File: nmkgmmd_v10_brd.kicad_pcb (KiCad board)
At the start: 2 copper layers, 85 x 69 mm, 148 parts, among them J1 CONN_01X05, J10 CONN_01X10, J14 CONN_01X10, J15 CONN_01X01, J16 CONN_01X01, J17 CONN_01X01, J18 CONN_01X01, J2 CONN_01X03, J20 CONN_01X10, J21 CONN_01X01, J22 CONN_01X01, J23 CONN_01X01, J24 CONN_01X01, J3 CONN_01X03, J4 CONN_01X04, J5 CONN_01X04, J6 CONN_01X04, J7 CONN_01X03, J8 CONN_01X03, J9 CONN_01X10, Q1 BSS138PS, Q10 PSMN1R0-40YLD, Q11 PSMN1R0-40YLD, Q12 PSMN1R0-40YLD, Q13 PSMN1R0-40YLD, Q14 PSMN1R0-40YLD, Q15 PSMN1R0-40YLD, Q16 PSMN1R0-40YLD, Q17 PSMN1R0-40YLD, Q2 PSMN1R0-40YLD, Q3 PSMN1R0-40YLD, Q4 PSMN1R0-40YLD, Q5 PSMN1R0-40YLD, Q6 PSMN1R0-40YLD, Q7 PSMN1R0-40YLD, Q8 PSMN1R0-40YLD, Q9 PSMN1R0-40YLD, SW1 SKRPACE010, SW2 SW_DPDT_x2, U1 STM32F303CCTx, U2 MCP16301, U3 MCP16301, U4 A4957, U5 ACS711, U6 A4957, U7 ACS711, Y1 Crystal

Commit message: 進捗，セーブ
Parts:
- added C33: C, Capacitors_SMD:C_0603, F.Cu at (61.0, 153.0)
- added C34: C, Capacitors_SMD:C_0603, F.Cu at (59.0, 153.0)
- added C35: C, Capacitors_SMD:C_0603, F.Cu at (63.0, 153.0)
- added C36: C, Capacitors_SMD:C_0603, F.Cu at (47.0, 105.0)
- added C37: C, Capacitors_SMD:C_0603, F.Cu at (47.0, 107.0)
- added C38: C, Capacitors_SMD:C_0603, F.Cu at (47.0, 103.0)
- C1, C10, C11, C12, C13, C14, C15, C16, C20, C31, C4, C5, C7, C8, C9, D1, D2, D6, D7, D8, D9, L3, L4, R1, R14, R15, R16, R17, R18, R19, R2, R27, R28, R29, R30, R31, R32, U2, U3: moved to B.Cu
- C23: moved to F.Cu
- J1: footprint Connectors_JST:JST_ZH_S05B-ZR_05x1.50mm_Angled -> Connectors_JST:JST_SH_BM05B-SRSS-TB_05x1.00mm_Straight; moved to B.Cu
- J6: footprint Connectors_JST:JST_ZH_S04B-ZR_04x1.50mm_Angled -> Connectors_JST:JST_ZH_B04B-ZR_04x1.50mm_Straight; moved to B.Cu
- moved R18 81.4 mm to (77.4, 151.2), turned to 180 degrees
- moved R17 80.2 mm to (80.0, 151.2), turned to 180 degrees
- moved R16 78.3 mm to (77.4, 141.2), turned to 180 degrees
- moved R13 76.0 mm to (91.8, 153.2), turned to 0 degrees
- moved C14 74.3 mm to (81.9, 148.6)
- moved C12 73.6 mm to (76.7, 148.4), turned to 270 degrees
- moved R15 70.5 mm to (80.0, 141.2), turned to 180 degrees
- moved C16 69.4 mm to (87.0, 151.0), turned to 0 degrees
- moved C11 68.9 mm to (76.7, 138.6), turned to 270 degrees
- moved R14 68.5 mm to (92.3, 150.9), turned to 270 degrees
- moved U3 68.3 mm to (79.4, 148.6)
- moved D9 68.0 mm to (83.2, 151.0), turned to 0 degrees
- moved C1 67.5 mm to (76.8, 98.7), turned to 0 degrees
- moved C13 66.4 mm to (81.9, 138.6)
- moved D8 65.9 mm to (83.2, 141.0), turned to 0 degrees
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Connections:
- R4 pad 2: Net-(J3-Pad3) -> Net-(J2-Pad3)
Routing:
- net GND: track 151.6 -> 242.9 mm, vias 50 -> 59
- net V_BATT: track 108.6 -> 176.4 mm, vias 1 -> 4
- net /MCU/T3_CH1: track 0.00 -> 48.5 mm
- net /MCU/T3_CH2: track 0.00 -> 47.1 mm, vias 0 -> 1
- net /MCU/T8_CH2N: track 0.00 -> 38.4 mm, vias 0 -> 1
- net Net-(SW2-Pad2): track 0.00 -> 35.8 mm, vias 0 -> 3
- net /MCU/A1_IN2: track 0.00 -> 35.7 mm, vias 0 -> 1
- net /MCU/FAULT2: track 0.00 -> 33.9 mm, vias 0 -> 3
- net /MCU/T8_CH1N: track 0.00 -> 33.6 mm, vias 0 -> 1
- net /MCU/A1_IN1: track 0.00 -> 32.1 mm, vias 0 -> 1
- net /MCU/T1_CH2: track 0.00 -> 27.9 mm, vias 0 -> 1
- net NRST: track 0.00 -> 27.6 mm, vias 0 -> 2
- net /MCU/T1_CH1: track 0.00 -> 26.9 mm, vias 0 -> 1
- net +3V3: track 56.2 -> 81.6 mm
- net /MCU/A3_IN1: track 0.00 -> 24.8 mm, vias 0 -> 1
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- added copper zone on B.Cu, net +3V3
- added copper zone on B.Cu, net +5V
- added copper zone on B.Cu, net Net-(C13-Pad1)
- added copper zone on B.Cu, net Net-(C13-Pad2)
- added copper zone on B.Cu, net Net-(C14-Pad1)
- added copper zone on B.Cu, net Net-(C14-Pad2)
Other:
- outline, holes or cut-outs redrawn

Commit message: 進捗
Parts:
- L1: moved to B.Cu
- R14: moved to F.Cu
- moved L1 36.4 mm to (105.4, 104.6)
- moved J3 33.0 mm to (105.4, 135.8)
- moved J7 33.0 mm to (105.4, 102.8)
- moved J2 33.0 mm to (105.4, 142.4)
- moved J8 33.0 mm to (105.4, 109.4)
- moved C12 16.7 mm to (88.2, 136.3)
- moved C14 16.7 mm to (93.4, 136.5)
- moved C16 16.7 mm to (98.5, 138.9)
- moved D1 16.7 mm to (101.0, 138.3)
- moved D7 16.7 mm to (90.0, 133.4)
- moved D9 16.7 mm to (94.8, 138.9)
- moved L4 16.7 mm to (97.1, 135.0)
- moved R1 16.7 mm to (101.0, 135.6)
- moved R17 16.7 mm to (91.5, 139.2)
- moved R18 16.7 mm to (88.9, 139.2)
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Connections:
- J3 pad 1: +5V -> GND
- J3 pad 2: GND -> +5V
- J5 pad 2: /MCU/T3_CH1 -> /MCU/T3_CH2
- J5 pad 3: /MCU/T3_CH2 -> /MCU/T3_CH1
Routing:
- net +5V: track 13.3 -> 57.7 mm, vias 0 -> 1
- net Net-(J2-Pad3): track 0.00 -> 41.6 mm, vias 0 -> 1
- net /MCU/A1_IN2: track 35.7 -> 1.50 mm, vias 1 -> 0
- net /MCU/A1_IN1: track 32.1 -> 2.31 mm
- net GND: track 242.9 -> 261.5 mm
- net Net-(J3-Pad3): track 0.00 -> 18.2 mm
- net +3V3: track 81.6 -> 92.8 mm, vias 2 -> 3
- net Net-(J7-Pad2): track 2.40 -> 9.75 mm
- net Net-(R22-Pad1): track 0.00 -> 6.00 mm
- net V_BATT: track 176.4 -> 181.3 mm, vias 4 -> 5
- net Net-(C14-Pad2): track 3.80 -> 8.53 mm
- net /MCU/FAULT1: track 21.6 -> 19.6 mm
- net /MCU/T1_CH1: track 26.9 -> 24.9 mm
- net /MCU/T3_CH1: track 48.5 -> 46.7 mm
- net Net-(SW2-Pad2): track 35.8 -> 37.4 mm
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- added copper zone on F.Cu, net Net-(C21-Pad2)
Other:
- board text added: "+5V"
- board text added: "GND"

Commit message: 進捗
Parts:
- C6, R7, R8, R9: moved to B.Cu
- moved J1 18.7 mm to (101.0, 92.0), turned to 180 degrees
- moved SW1 17.1 mm to (93.5, 91.1), turned to 180 degrees
- moved C1 16.2 mm to (92.2, 93.8), turned to 180 degrees
- moved C5 6.91 mm to (99.9, 111.9)
- moved C4 6.91 mm to (101.3, 111.9)
- moved C7 6.90 mm to (97.2, 103.1)
- moved C8 6.90 mm to (87.9, 105.7)
- moved U1 6.90 mm to (93.9, 109.0)
- moved R12 6.79 mm to (101.8, 109.3), turned to 180 degrees
- moved D3 6.50 mm to (102.1, 121.7), turned to 90 degrees
- moved D4 6.50 mm to (100.6, 121.7), turned to 90 degrees
- moved D5 6.50 mm to (99.1, 121.7), turned to 90 degrees
- moved C6 3.94 mm to (99.1, 114.9), turned to 180 degrees
- moved R7 3.92 mm to (102.1, 118.9), turned to 270 degrees
- moved R8 3.92 mm to (100.6, 118.9), turned to 270 degrees
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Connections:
- J4 pad 2: /MCU/T2_CH1 -> /MCU/T2_CH2
- J4 pad 3: /MCU/T2_CH2 -> /MCU/T2_CH1
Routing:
- net +3V3: track 92.8 -> 132.1 mm, vias 3 -> 4
- net /MCU/A1_IN2: track 1.50 -> 37.1 mm, vias 0 -> 2
- net /MCU/RESET2: track 2.04 -> 21.9 mm, vias 1 -> 3
- net Net-(J2-Pad3): track 41.6 -> 24.2 mm, vias 1 -> 0
- net /MCU/T1_CH1N: track 8.12 -> 22.3 mm, vias 1 -> 3
- net /MCU/LED1: track 13.9 -> 0.00 mm, vias 1 -> 0
- net /MCU/A1_IN1: track 2.31 -> 15.5 mm, vias 1 -> 2
- net Net-(R12-Pad2): track 9.05 -> 2.94 mm
- net /MCU/T2_CH1: track 18.2 -> 13.3 mm, vias 2 -> 1
- net /MCU/LED0: track 16.4 -> 13.2 mm, vias 1 -> 2
- net /MCU/T1_CH2N: track 23.9 -> 20.8 mm
- net /MCU/T1_CH1: track 24.9 -> 22.0 mm
- net /MCU/FAULT1: track 19.6 -> 17.1 mm
- net /MCU/T2_CH2: track 17.1 -> 14.5 mm, vias 0 -> 1
- net NRST: track 27.6 -> 30.1 mm
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- added copper zone on F.Cu, net Net-(C22-Pad2)
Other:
- board text added: "+3V3"
- board text added: "AN1"
- board text added: "AN2"

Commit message: 進捗
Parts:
- R10, R11: moved to B.Cu
- moved R10 101.4 mm to (169.1, 69.4), turned to 270 degrees
- moved R11 99.5 mm to (169.1, 72.0), turned to 270 degrees
- moved J6 97.1 mm to (170.0, 84.5)
- moved L2 96.1 mm to (175.9, 83.7)
- moved C9 96.1 mm to (177.8, 84.5)
- moved C10 96.1 mm to (179.2, 84.5)
- moved C2 95.6 mm to (181.6, 89.2), turned to 90 degrees
- moved Y1 94.8 mm to (182.3, 86.0)
- moved J8 94.3 mm to (191.4, 70.8)
- moved C8 92.8 mm to (174.8, 73.0), turned to 45 degrees
- moved C7 92.7 mm to (184.3, 71.5), turned to 315 degrees
- moved C4 92.1 mm to (187.7, 79.9)
- moved C5 92.1 mm to (186.3, 79.9)
- moved C6 92.1 mm to (185.5, 82.9)
- moved U1 92.1 mm to (180.3, 77.0)
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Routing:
- net GND: track 259.2 -> 315.4 mm, vias 60 -> 75
- net /MCU/A3_IN1: track 24.8 -> 5.33 mm, vias 1 -> 0
- net V_BATT: track 181.3 -> 200.1 mm, vias 5 -> 4
- net /MCU/A1_IN2: track 37.1 -> 21.9 mm
- net +3V3: track 132.1 -> 146.4 mm
- net /MCU/LED1: track 0.00 -> 12.0 mm, vias 0 -> 2
- net /MCU/LED2: track 7.77 -> 14.5 mm, vias 0 -> 2
- net /MCU/RESET2: track 21.9 -> 27.9 mm, vias 3 -> 1
- net /MCU/T1_CH2: track 24.4 -> 19.1 mm
- net /MCU/T1_CH1: track 22.0 -> 17.3 mm
- net /MCU/T1_CH2N: track 20.8 -> 16.7 mm
- net /MCU/FAULT1: track 17.1 -> 13.0 mm
- net /MCU/LED0: track 13.2 -> 17.2 mm
- net /MCU/T8_CH1N: track 34.5 -> 30.6 mm
- net /MCU/T8_CH2N: track 37.8 -> 34.1 mm
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
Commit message: ネットリスト更新，進捗
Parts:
- moved C10 1.00 mm to (179.2, 83.5)
- moved C4 1.00 mm to (187.7, 78.9)
- moved C5 1.00 mm to (186.3, 78.9)
- moved C6 1.00 mm to (185.5, 81.9)
- moved C7 1.00 mm to (184.3, 70.5)
- moved C8 1.00 mm to (174.8, 72.0)
- moved C9 1.00 mm to (177.8, 83.5)
- moved L2 1.00 mm to (175.9, 82.7)
- moved R12 1.00 mm to (187.1, 76.2)
- moved U1 1.00 mm to (180.3, 76.0)
- moved Y1 1.00 mm to (182.3, 85.0)
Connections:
- J10 pad 1: /MCU/A2_IN12 -> /MCU/A3_IN1
- J9 pad 1: /MCU/A3_IN1 -> /MCU/A2_IN12
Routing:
- net /MCU/A2_IN12: track 0.00 -> 16.8 mm, vias 0 -> 1
- net /MCU/A3_IN1: track 5.33 -> 20.4 mm, vias 0 -> 1
- net GND: track 315.4 -> 325.1 mm, vias 75 -> 77
- net /MCU/T8_CH1N: track 30.6 -> 27.9 mm
- net /MCU/A1_IN2: track 21.9 -> 19.8 mm, vias 2 -> 1
- net /MCU/T8_CH2N: track 34.1 -> 32.2 mm
- net /MCU/T1_CH1: track 17.3 -> 18.7 mm
- net +3V3: track 146.4 -> 147.8 mm
- net /MCU/T1_CH2: track 19.1 -> 20.5 mm
- net SWCLK: track 17.3 -> 16.2 mm
- net /MCU/T1_CH1N: track 20.7 -> 19.6 mm
- net SWDIO: track 13.0 -> 12.0 mm
- net NRST: track 31.2 -> 30.2 mm
- net /MCU/T8_CH2: track 21.2 -> 22.2 mm
- net /MCU/T8_CH1: track 19.8 -> 20.8 mm
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
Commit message: 進捗
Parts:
- moved Q1 13.0 mm to (170.5, 84.1), turned to 180 degrees
- moved R6 12.7 mm to (173.0, 83.3), turned to 90 degrees
- moved R5 11.7 mm to (168.1, 82.9), turned to 90 degrees
- moved R4 11.0 mm to (170.2, 86.3), turned to 0 degrees
- moved J6 10.5 mm to (170.0, 74.0)
- moved R3 9.14 mm to (168.1, 85.4), turned to 90 degrees
- moved R10 8.04 mm to (177.0, 67.9)
- moved R11 6.77 mm to (174.9, 68.5), turned to 180 degrees
- moved C2 4.77 mm to (177.6, 86.6)
- moved Y1 2.62 mm to (180.3, 86.7)
- moved C3 2.50 mm to (183.0, 86.7)
- moved C16 2.47 mm to (182.2, 106.3)
- moved D9 2.47 mm to (178.3, 106.3)
- moved R18 2.47 mm to (172.5, 106.5)
- moved C14 2.47 mm to (177.0, 103.9)
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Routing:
- net GND: track 325.1 -> 385.2 mm, vias 77 -> 90
- net +5V: track 57.7 -> 102.4 mm
- net Net-(R21-Pad1): track 0.00 -> 26.2 mm
- net Net-(R32-Pad2): track 0.00 -> 23.5 mm
- net /MCU/T15_CH2: track 0.00 -> 22.0 mm, vias 0 -> 1
- net /MCU/T4_CH2: track 1.27 -> 20.6 mm, vias 1 -> 3
- net Net-(J3-Pad3): track 18.2 -> 35.8 mm
- net Net-(J2-Pad3): track 24.2 -> 41.0 mm
- net Net-(R31-Pad2): track 0.00 -> 14.5 mm
- net +3V3: track 147.8 -> 161.2 mm, vias 4 -> 5
- net /MCU/A4_IN3: track 10.7 -> 4.43 mm
- net Net-(R22-Pad1): track 6.00 -> 11.4 mm
- net Net-(Q8-Pad4): track 0.00 -> 3.82 mm, vias 0 -> 1
- net Net-(Q6-Pad4): track 0.00 -> 3.82 mm, vias 0 -> 1
- net /MCU/U2_RX: track 7.09 -> 10.5 mm
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
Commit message: 進捗
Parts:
- added Q18: BSS138, TO_SOT_Packages_SMD:SOT-23, F.Cu at (172.6, 82.6)
- Q1: value BSS138PS -> BSS138; footprint TO_SOT_Packages_SMD:SOT-363_SC-70-6 -> TO_SOT_Packages_SMD:SOT-23
- moved R5 6.17 mm to (169.0, 76.8), turned to 180 degrees
- moved Q1 5.04 mm to (169.0, 79.3), turned to 270 degrees
- moved R4 4.66 mm to (169.0, 81.8), turned to 180 degrees
- moved R3 4.51 mm to (172.6, 85.1), turned to 180 degrees
- moved R6 3.22 mm to (172.6, 80.1), turned to 180 degrees
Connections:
- Q1 pad 1: /MCU/T4_CH2 -> +3V3
- Q1 pad 2: +3V3 -> /MCU/T4_CH2
- R5 pad 2: /MCU/T15_CH2 -> /MCU/T4_CH2
- R6 pad 2: /MCU/T4_CH2 -> /MCU/T15_CH2
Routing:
- net GND: track 385.2 -> 723.1 mm, vias 90 -> 168
- net +5V: track 102.4 -> 110.2 mm, vias 1 -> 4
- net /MCU/T4_CH2: track 20.6 -> 15.3 mm, vias 3 -> 1
- net Net-(J2-Pad3): track 41.0 -> 46.0 mm
- net /MCU/T15_CH2: track 22.0 -> 19.7 mm, vias 1 -> 3
- net +3V3: track 161.2 -> 163.3 mm, vias 5 -> 7
- net Net-(J3-Pad3): track 35.8 -> 36.6 mm
- net Net-(SW2-Pad2): track 36.9 -> 37.5 mm

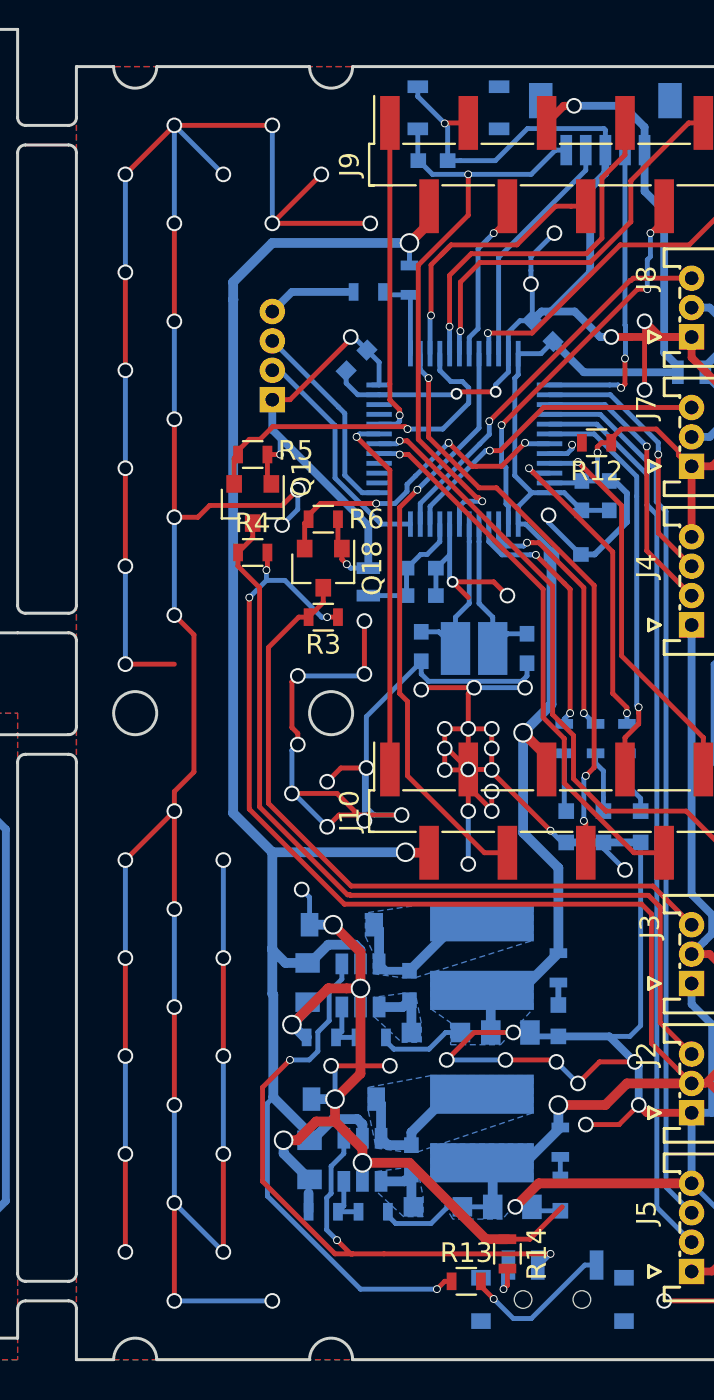
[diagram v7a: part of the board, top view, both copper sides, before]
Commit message: ネットリスト更新 配線編集
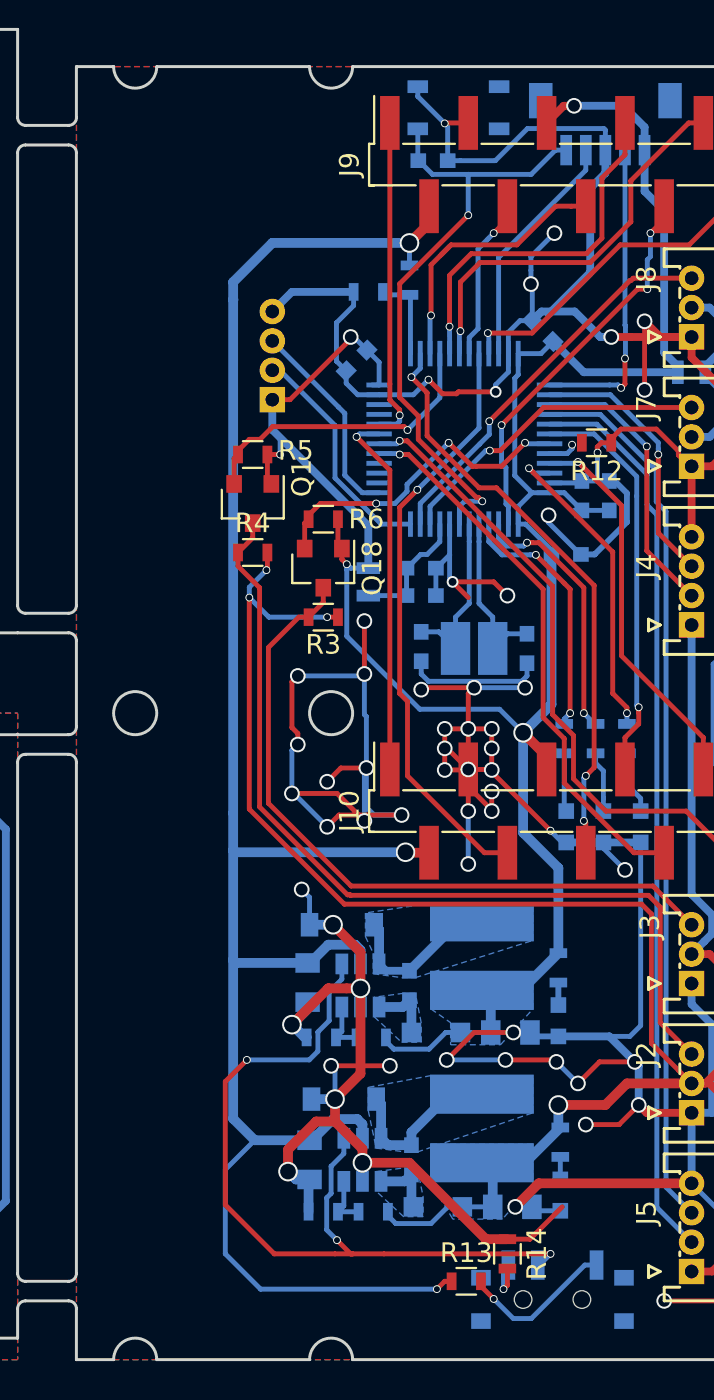
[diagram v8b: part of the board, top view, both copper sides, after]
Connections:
- Q1 pad 2: /MCU/T4_CH2 -> /MCU/T15_CH2
- Q18 pad 2: /MCU/T15_CH2 -> /MCU/T4_CH2
- R5 pad 2: /MCU/T4_CH2 -> /MCU/T15_CH2
- R6 pad 2: /MCU/T15_CH2 -> /MCU/T4_CH2
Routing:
- net GND: track 723.1 -> 552.0 mm, vias 168 -> 132
- net +3V3: track 163.3 -> 178.1 mm
- net V_BATT: track 202.5 -> 209.9 mm
- net Net-(SW2-Pad2): track 37.5 -> 42.1 mm
- net /MCU/T15_CH2: track 19.7 -> 15.6 mm, vias 3 -> 1
- net /MCU/T4_CH2: track 15.3 -> 16.8 mm, vias 1 -> 3
- net NRST: track 31.3 -> 32.1 mm
- net +5V: track 110.2 -> 110.8 mm
